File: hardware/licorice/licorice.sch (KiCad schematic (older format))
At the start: 110 parts, among them P1 TX-IN, P10 CONN_1, P11 CONN_1, P12 CONN_1, P2 TX/RX, P3 RX-only, P4 SERIAL, P5 RX-OUT, P6 CLK, P7 SWITCH_CTRL, P8 VCC, P9 CONN_1, T1 TX_IF_BALUN, T2 TX_BALUN, T3 RX_BALUN, T8 RX_IF_BALUN, U1 RFFC5071, U10 SKY13350, U11 RX_HIGHPASS_FILTER, U12 SKY13350, U13 RX_LOWPASS_FILTER, U14 SKY13350, U15 SKY13350, U17 GSG-74HC04, U2 SKY13350, U3 SKY13350, U4 SKY13350, U5 TX_LOWPASS_FILTER, U6 SKY13350, U7 SKY13350, U8 TX_HIGHPASS_FILTER, U9 SKY13350

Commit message: reworked licorice for half-duplex only. switch control signals not done yet
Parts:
- removed C10, C11, C15, C24, C35, C39, C7, C9: 10nF, symbol C
- removed C12, C13, C2, C25, C27, C32, C36, C38, C41, C43, C46, C48, C49, C8: 33pF, symbol C
- removed C14, C22: 100pF, symbol C
- removed C23, C26, C5, C67: 47pF, symbol C
- removed C42: 2.2nF, symbol C
- removed D1: GSG-DIODE-TVS-BI, symbol GSG-DIODE-TVS-BI
- removed L1, L2: 180nH, symbol INDUCTOR
- removed L3: DNP, symbol INDUCTOR
- removed L4, L5: 47nH, symbol INDUCTOR
- removed P3: RX-only, symbol GSG-SMA-CONN
- removed T1: TX_IF_BALUN, symbol BALUN
- removed T8: RX_IF_BALUN, symbol BALUN
- removed U1: RFFC5071, symbol RFFC5071
- removed U14, U3, U4, U6, U7, U9: SKY13350, symbol SKY13350
- removed U5: TX_LOWPASS_FILTER, symbol FIL-LP0603
- removed U8: TX_HIGHPASS_FILTER, symbol FIL-DEA
- added C? (x2): 33pF, symbol C
- added C? (x5): 10nF, symbol C
- added C? (x2): 47pF, symbol C
- added L?: DNP, symbol INDUCTOR
- added L? (x2): 180nH, symbol INDUCTOR
- added U? (x3): SKY13350, symbol SKY13350
- added U?: SKY13317, symbol SKY13317
- added U?: RFFC5072, symbol RFFC5072
- L6: value 3n3 -> DNP; Description INDUCTOR 3.3NH 300MA 0402 -> (none); Manufacturer Murata -> (none); Part Number LQG15HS3N3S02D -> (none)
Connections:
- wire segments 349 -> 327
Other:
- note added: "switchable image reject filters"
- note removed: "antenna diversity switches"
- note removed: "switchable RX image reject filters"
- note removed: "switchable TX image reject filters"
- moved on the sheet: C1, C16, C17, C18, C19, C20, C21, C28, C29, C3, C30, C31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

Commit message: added amplification
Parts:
- added C? (x2): 10nF, symbol C
- added C? (x6): 100pF, symbol C
- added C? (x2): 1uF, symbol C
- added L? (x2): 180nH, symbol INDUCTOR
- added U? (x2): SKY13317, symbol SKY13317
- added U? (x2): MGA-81563, symbol MGA-81563
- P2: value TX/RX -> ANTENNA
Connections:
- net GND: now also U?.0 (GND), C?.2, C?.2, C?.2, C?.2, U?.0 (GND), U?.0 (GND), U?.1 (GND), U?.1 (GND), U?.2 (GND), U?.2 (GND), U?.4 (GND), U?.4 (GND), U?.5 (GND), U?.5 (GND)
- net VCC: now also C?.1, C?.1, C?.1, C?.1, L?.2, L?.2
- net at D2.2 (K), P2.1 (RF): now also C?.1; no longer C37.1
- new net: C37.1, U?.1 (RFC)
- new net: C?.1, U?.4 (RF1)
- new net: C?.1, U?.5 (RF2)
- new net: C?.2, U?.8 (RF3)
- new net: C?.2, U?.1 (RFC)
- new net: C?.2, U?.4 (RF1)
- new net: C?.2, U?.5 (RF2)
- new net: C?.1, U?.8 (RF3)
- new net: C?.1, L?.1, U?.6 (OUT)
- new net: C?.1, U?.3 (IN)
- new net: C?.2, U?.3 (IN)
- new net: C?.2, L?.1, U?.6 (OUT)
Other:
- note added: "RX amp"
- note added: "TX amp"
- note added: "no amp"
- moved on the sheet: C37, D2, P2

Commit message: one amp, not two
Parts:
- removed C?: 10nF, symbol C
- removed C?: 1uF, symbol C
- removed C? (x3): 100pF, symbol C
- removed L?: 180nH, symbol INDUCTOR
- removed U?: MGA-81563, symbol MGA-81563
- added C? (x2): 100pF, symbol C
- added C?: 10nF, symbol C
- added Q?: MOSFET_P, symbol MOSFET_P
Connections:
- net VCC: now also Q?.S; no longer C?.1, C?.1, L?.2
- net at U?.4 (RF1): now also C?.2
- net TX_AMP_IN: now reaches U?.5 (RF2)
- net TX_AMP_IN: now also C?.2
- net RX_AMP_OUT: now reaches C?.2, U?.8 (RF3)
- net at C?.2: now also C?.1, L?.2, U?.6 (OUT); no longer U?.4 (RF1)
- net RX_AMP_IN: now reaches U?.5 (RF2)
- net RX_AMP_IN: now also C?.1
- net AMP_BYPASS: now reaches U?.8 (RF3)
- net AMP_BYPASS: now also C?.1
- net at U?.3 (IN): now also C?.1, C?.2; no longer C?.1
- new net: C?.1, C?.1, L?.1, Q?.D
- new net AMP_PWR: Q?.G
- new net TX_AMP_OUT: C?.1, U?.4 (RF1)
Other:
- note removed: "RX amp"
- note removed: "TX amp"
- note removed: "no amp"
- moved on the sheet: C?, D2, L?, P2, U?

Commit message: switch control signals
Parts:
- added C10, C19, C24, C28, C37, C38, C39, C44, C52, C53, C54, C58, C61, C63, C64: 33pF, symbol C
- added C67: 100nF, symbol C
- added U16: GSG-74HC08, symbol GSG-74HC08
- gave numbers to parts that had none: 30
- renumbered C16 to C1, C40 to C11, C28 to C12, C29 to C13, C30 to C14, C31 to C15, C6 to C16, C34 to C17, C33 to C18, C17 to C2, C45 to C20, C3 to C21, C59 to C25, C44 to C26, C58 to C29, C18 to C3, C54 to C33, C55 to C34, C56 to C35, C57 to C36, C19 to C4, C61 to C40, C62 to C41, C37 to C43, C47 to C46, C51 to C47, C50 to C49, C20 to C5, C52 to C55, C21 to C6, C74 to C65, C69 to C66, C77 to C68, C1 to C7, C4 to C8, D2 to D1, L6 to L4, P11 to P10, P12 to P11, P4 to P2, P5 to P3, P2 to P4, P6 to P5, P7 to P6, P8 to P7, P9 to P8, P10 to P9, T3 to T1, U2 to U1, U15 to U11, U17 to U15, U13 to U3, U10 to U5, U12 to U6, U11 to U8
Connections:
- net !RX_BYPASS is gone; now on net !MIX_BYPASS: C46.2, U11.5 (VCTL2), U15.4 (2Y)
- net !TX_ANT is gone; now on net RX: U15.10 (5Y)
- net RX_HP is gone; now on net HP: P6.9, U15.9 (4A)
- net RX_LP is gone; now on net LP: U15.8 (4Y)
- net AMP_BYPASS: now also P6.3 (P3), U12.3 (V1), U12.7 (V3), U14.6 (V2), U14.7 (V3), U15.5 (3A), C53.1, C58.2, C63.2, C64.2, U16.11 (4Y); no longer C59.1, U14.8 (RF3)
- net GND: now also U10.3 (GND), C10.1, C19.1, C24.1, C28.2, C37.1, C38.1, C39.1, C44.1, C52.2, C53.2, C54.2, C58.1, C61.2, C63.1, C64.1, C67.2, U16.0, U16.7 (GND)
- net VCC: now also U15.1 (1A), C67.1, U16.14 (VCC)
- net at D1.2 (K), P4.1 (RF): now also C62.2; no longer C62.1
- net LP: now reaches U5.1 (VCTL1)
- net LP: now also C11.2, U6.5 (VCTL2), C19.2
- net HP: now reaches U5.5 (VCTL2)
- net HP: now also C29.1, U6.1 (VCTL1), C28.1
- net RX: now reaches C22.2, U7.1 (VCTL1)
- net RX: now also U10.1 (VCTL1), U2.1 (VCTL1), C10.2, C52.1, U16.12 (4A), U16.2 (1B)
- net TX: now reaches C32.1, U7.5 (VCTL2)
- net TX: now also P6.5 (P5), U10.5 (VCTL2), U15.11 (5A), U2.5 (VCTL2), C24.2, C44.2, U16.5 (2B), U16.9 (3A)
- net TX_MIX_BP: now reaches U9.3 (V1)
- net TX_MIX_BP: now also C38.2, U16.6 (2Y)
- net !MIX_BYPASS: now reaches U9.6 (V2)
- net !MIX_BYPASS: now also C16.1, U1.1 (VCTL1), C37.2
- net RX_MIX_BP: now reaches U9.7 (V3)
- net RX_MIX_BP: now also C39.2, U16.3 (1Y)
- net TX_AMP: now reaches U12.6 (V2)
- net TX_AMP: now also U14.3 (V1), C54.1, C61.1, U16.8 (3Y)
- net at U14.1 (RFC): now also C62.1; no longer C62.2
- removed net !TX_BYPASS: C16.1, U1.1 (VCTL1), U15.2 (1Y)
- net AMP_PWR renamed !AMP_PWR
- net !AMP_PWR: now also P6.11
- net RX_BYPASS renamed MIX_BYPASS
- net MIX_BYPASS: now also C7.2, P6.1 (P1), U1.5 (VCTL2), U16.1 (1A), U16.4 (2A); no longer P6.3 (P3)
- removed net TX_ANT: P6.11, U15.11 (5A)
- removed net TX_BYPASS: C7.2, P6.1 (P1), U1.5 (VCTL2), U15.1 (1A)
- removed net TX_HP: C29.1, P6.5 (P5), U15.5 (3A), U6.1 (VCTL1)
- removed net TX_LP: C11.2, U15.6 (3Y), U6.5 (VCTL2)
- new net: C59.1, U14.8 (RF3)
- new net !AMP_BYPASS: U15.6 (3Y), U16.10 (3B), U16.13 (4B)
- no-connect marks 8 -> 9
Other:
- moved on the sheet: C23, C30, C31, C32, C42, C43, C48, C50, C51, C56, C57, C59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

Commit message: module selection
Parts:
- Q1: Description (none) -> MOSFET P-CH 50V 130MA SOT-23; Manufacturer (none) -> Fairchild; Part Number (none) -> BSS84
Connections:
- net AMP_BYPASS: no longer C53.1, C63.2, U12.7 (V3), U14.6 (V2), U16.11 (4Y)
- new net RX_AMP: C53.1, C63.2, U12.7 (V3), U14.6 (V2), U16.11 (4Y)
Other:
- moved on the sheet: C46, C47, C49, C55, P3, U11

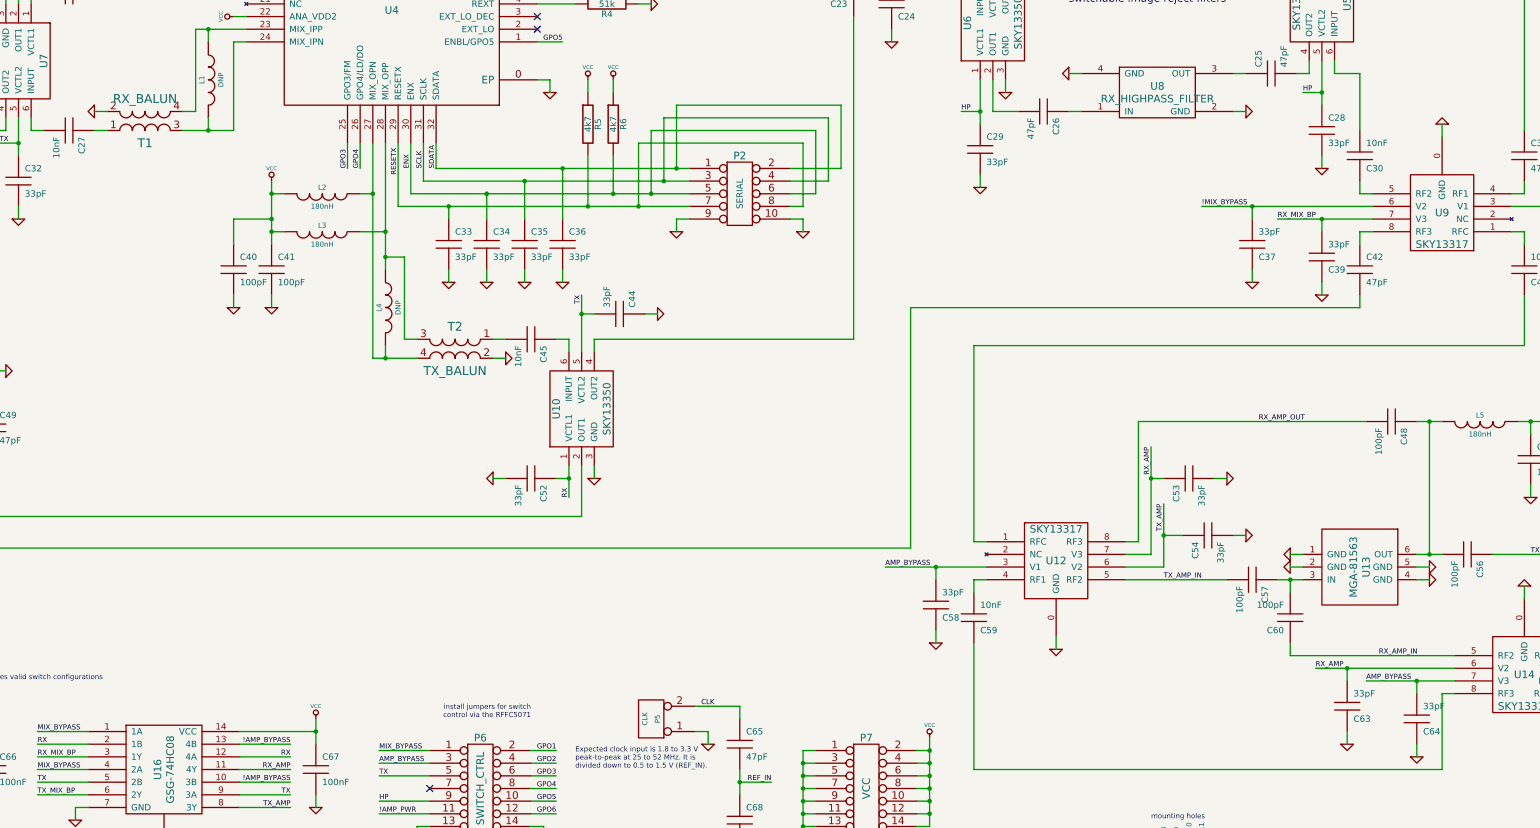
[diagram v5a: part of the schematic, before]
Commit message: started module placement
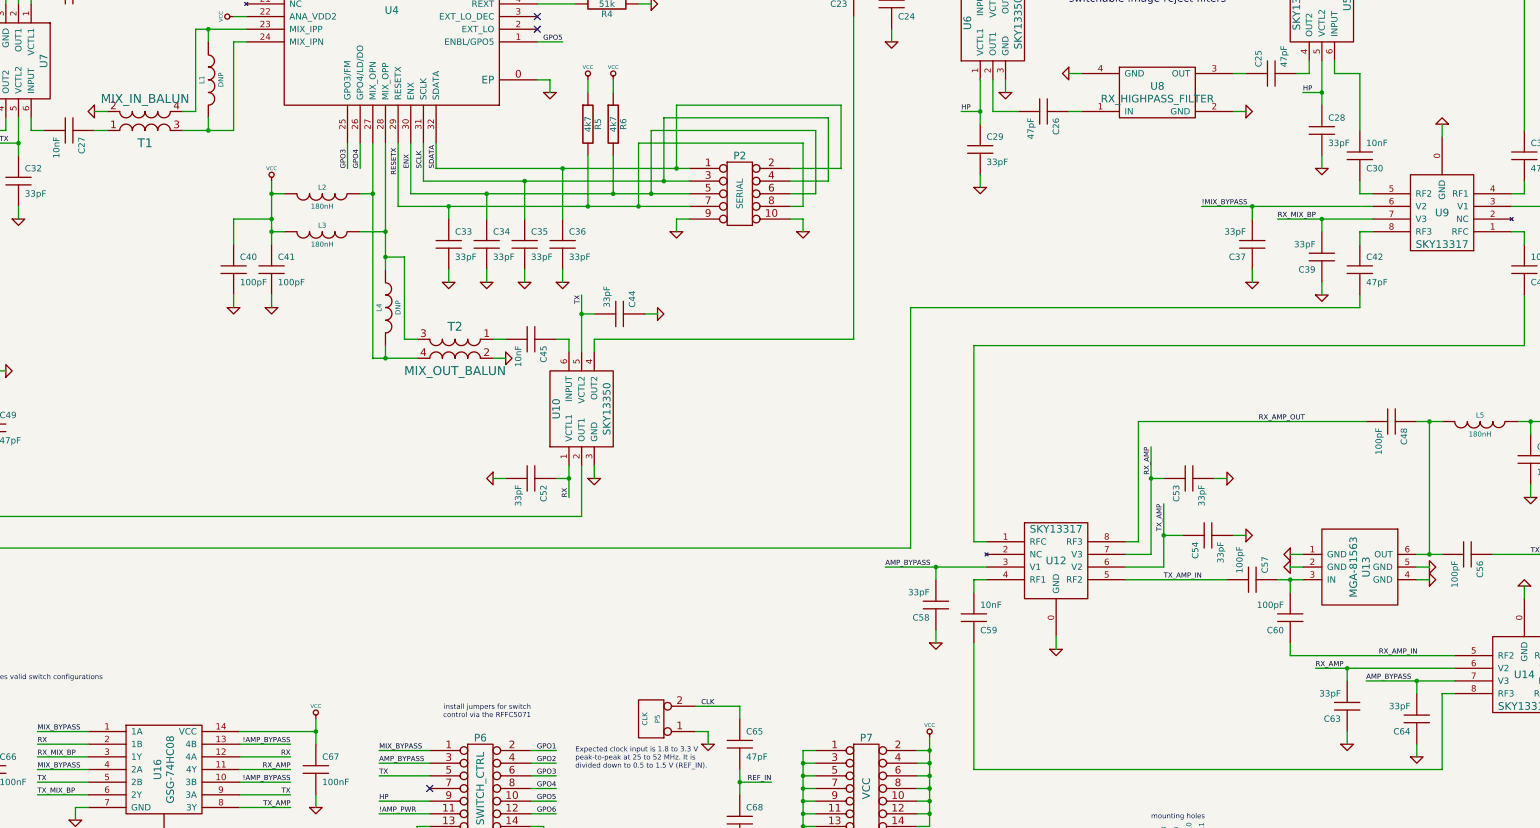
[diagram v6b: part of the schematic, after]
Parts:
- T1: value RX_BALUN -> MIX_IN_BALUN
- T2: value TX_BALUN -> MIX_OUT_BALUN
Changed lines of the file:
@@
-EESchema Schematic File Version 2  date Fri Aug 17 13:08:20 2012
+EESchema Schematic File Version 2  date Fri Aug 17 14:06:50 2012
 LIBS:power
 LIBS:device
@@
 F 6 "CAP CER 33PF 50V 5% NP0 0402" H 21250 10550 60  0001 C CNN "Description"
 	1    9900 8300
-	1    0    0    1
+	-1   0    0    1
 $EndComp
 Text Label 15300 8400 3    40   ~ 0
@@
 F 6 "CAP CER 33PF 50V 5% NP0 0402" H 25050 11450 60  0001 C CNN "Description"
 	1    13700 9200
-	1    0    0    1
+	-1   0    0    1
 $EndComp
 $Comp
@@
 F 6 "CAP CER 33PF 50V 5% NP0 0402" H 24500 11350 60  0001 C CNN "Description"
 	1    13150 9100
-	1    0    0    1
+	-1   0    0    1
 $EndComp
 Text Label 13300 8900 0    40   ~ 0
@@
 F 6 "CAP CER 33PF 50V 5% NP0 0402" H 23750 7700 60  0001 C CNN "Description"
 	1    12400 5450
-	1    0    0    1
+	-1   0    0    1
 $EndComp
 $Comp
@@
 F 6 "CAP CER 33PF 50V 5% NP0 0402" H 24300 7800 60  0001 C CNN "Description"
 	1    12950 5550
-	1    0    0    1
+	-1   0    0    1
 $EndComp
 Text Label 15200 5150 2    40   ~ 0
@@
 F 6 "CAP CER 100PF 50V 5% NP0 0402" H 15400 9650 60  0001 C CNN "Description"
 	1    12400 8100
-	0    1    1    0
+	0    1    -1   0
 $EndComp
 $Comp
@@
 P 6100 6300
 F 0 "T2" H 6100 6500 70  0000 C CNN
-F 1 "TX_BALUN" H 6100 6150 70  0000 C CNN
+F 1 "MIX_OUT_BALUN" H 6100 6150 70  0000 C CNN
 	1    6100 6300
 	1    0    0    -1
@@
 P 3650 4450
 F 0 "T1" H 3650 4650 70  0000 C CNN
-F 1 "RX_BALUN" H 3650 4300 70  0000 C CNN
+F 1 "MIX_IN_BALUN" H 3650 4300 70  0000 C CNN
 	1    3650 4450
 	-1   0    0    1

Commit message: added series resistor to amp supply
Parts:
- added R7: 33, symbol R
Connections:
- net at C50.1, C51.1, L5.1: now also R7.2; no longer Q1.D
- new net: Q1.D, R7.1
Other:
- moved on the sheet: Q1

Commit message: fixed balun shorts
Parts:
- added C69, C70: 10nF, symbol C
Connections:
- net GND: now also C69.2, C70.1; no longer T1.2 (S2), T2.2 (S2)
- new net: C69.1, T1.2 (S2)
- new net: C70.2, T2.2 (S2)
